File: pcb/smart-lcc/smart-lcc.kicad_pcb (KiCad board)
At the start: 2 copper layers, 53.2 x 53.2 mm, 4 parts

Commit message: Work on PCB
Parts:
- added C1: 2.2 µF / 25V, Capacitor_SMD:C_1206_3216Metric, F.Cu at (62.5, 36.6)
- added C2: 4.7µF / 25V, X7R, Capacitor_SMD:C_1206_3216Metric, F.Cu at (62.6, 32.8)
- added C3: 0.1 µF / 25V, X7R, Capacitor_SMD:C_0603_1608Metric, F.Cu at (62.5, 30.6)
- added J3: Conn_01x24 (mirrored), Connector_FFC-FPC:Hirose_FH12-24S-0.5SH_1x24-1MP_P0.50mm_Horizontal, F.Cu at (49.6, 36.1)
- added R1: 2K2, Resistor_SMD:R_0402_1005Metric, F.Cu at (29.8, 36.4)
- added R2: 3K3, Resistor_SMD:R_0402_1005Metric, F.Cu at (32.3, 36.4)
- added R3: 910K, Resistor_SMD:R_0603_1608Metric, F.Cu at (62.5, 39.2)
- added REF**: MountingHole_2.7mm, MountingHole:MountingHole_2.7mm, F.Cu at (33.5, 25.0)
- added REF**: MountingHole_2.7mm, MountingHole:MountingHole_2.7mm, F.Cu at (65.4, 25.0)
- added REF**: MountingHole_2.7mm, MountingHole:MountingHole_2.7mm, F.Cu at (70.2, 70.0)
- added REF**: MountingHole_2.7mm, MountingHole:MountingHole_2.7mm, F.Cu at (28.7, 70.0)
- added U1: ABX00027, ABX00027:MODULE_ABX00027, F.Cu at (53.9, 53.5)
- J1: renamed from REF**; value PinHeader_1x06_P2.54mm_Vertical -> Control board connector
- J2: renamed from REF**; value PinHeader_1x06_P2.54mm_Vertical -> Aux connector
- SW1, SW2: renamed from REF**; value SW_Push_1P1T_NO_6x6mm_H9.5mm -> SW_Push; moved to B.Cu
- moved J2 38.2 mm to (56.5, 73.4), turned to 270 degrees
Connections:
- J1 pad 1: (no net) -> +12V
- J1 pad 2: (no net) -> TX_TO_CONTROL_BOARD
- J1 pad 3: (no net) -> RX_FROM_CONTROL_BOARD_5V
- J1 pad 4: (no net) -> GND
- J1 pad 5: (no net) -> 3V3_OLED
- J1 pad 6: (no net) -> 3V3_MCU
- J2 pad 1: (no net) -> +12V
- J2 pad 2: (no net) -> RX_FROM_AUX
- J2 pad 3: (no net) -> TX_TO_AUX
- J2 pad 4: (no net) -> GND
- J2 pad 5: (no net) -> 3V3_OLED
- J2 pad 6: (no net) -> 3V3_MCU
- SW1 pad 1: (no net) -> +3V3
- SW1 pad 2: (no net) -> SW_MINUS
- SW2 pad 1: (no net) -> +3V3
- SW2 pad 2: (no net) -> SW_PLUS
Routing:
- net +12V: track 0.00 -> 122.0 mm
- net 3V3_OLED: track 0.00 -> 61.8 mm, vias 0 -> 1
- net GND: track 0.00 -> 46.9 mm, vias 0 -> 5
- net +3V3: track 0.00 -> 43.6 mm, vias 0 -> 1
- net SSD1309_CS: track 0.00 -> 36.9 mm
- net SSD1309_MOSI: track 0.00 -> 33.0 mm
- net 3V3_MCU: track 0.00 -> 32.5 mm
- net RX_FROM_CONTROL_BOARD_3V3: track 0.00 -> 30.5 mm
- net SSD1309_SCLK: track 0.00 -> 28.6 mm, vias 0 -> 2
- net TX_TO_CONTROL_BOARD: track 0.00 -> 25.4 mm
- net SW_MINUS: track 0.00 -> 22.7 mm, vias 0 -> 1
- net TX_TO_AUX: track 0.00 -> 21.9 mm
- net SW_PLUS: track 0.00 -> 17.5 mm, vias 0 -> 1
- net RX_FROM_AUX: track 0.00 -> 14.1 mm
- net RX_FROM_CONTROL_BOARD_5V: track 0.00 -> 12.4 mm, vias 0 -> 1
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- added copper zone on In1.Cu, net GND
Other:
- copper layers 2 -> 4
- net class 12V added: clearance 0.4, trace_width 0.5, via_dia 1.6, via_drill 0.8

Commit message: WIP
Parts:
- C3: footprint Capacitor_SMD:C_0603_1608Metric -> Capacitor_SMD:C_1206_3216Metric
- J1: footprint Connector_PinHeader_2.54mm:PinHeader_1x06_P2.54mm_Vertical -> TE_280372-1:TE_280372-1
- R1, R2: footprint Resistor_SMD:R_0402_1005Metric -> Resistor_SMD:R_0603_1608Metric
- moved J1 6.32 mm to (25.9, 45.3), turned to 270 degrees
- moved R2 4.06 mm to (36.3, 36.4)
- moved R1 2.92 mm to (32.8, 36.4)
- moved C3 0.76 mm to (62.5, 29.8)
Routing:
- net RX_FROM_CONTROL_BOARD_5V: track 12.4 -> 15.0 mm
- net RX_FROM_CONTROL_BOARD_3V3: track 30.5 -> 29.8 mm

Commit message: WIP
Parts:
- added JP1: SolderJumper_2_Open, Jumper:SolderJumper-2_P1.3mm_Open_RoundedPad1.0x1.5mm, F.Cu at (57.3, 68.6)
- added JP2: SolderJumper_2_Bridged, Jumper:SolderJumper-2_P1.3mm_Bridged_RoundedPad1.0x1.5mm, F.Cu at (41.2, 68.6)
- J1: value Control board connector -> 280372-1
- moved J1 47.1 mm to (73.0, 45.5)
- moved R1 45.1 mm to (72.1, 58.4), turned to 90 degrees
- moved R2 43.1 mm to (71.2, 61.7), turned to 0 degrees
- moved U1 8.33 mm to (45.6, 52.8), turned to 0 degrees
- moved C2 0.27 mm to (62.5, 33.0), turned to 180 degrees
- turned C3 to 180 degrees
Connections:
- U1 pad 10: SSD1309_DC -> Net-(U1-Pad10)
- U1 pad 11: SSD1309_RES -> Net-(U1-Pad11)
- U1 pad 15: +12V -> VIN
- U1 pad 20: Net-(U1-Pad20) -> SSD1309_DC
- U1 pad 21: Net-(U1-Pad21) -> SSD1309_RES
- U1 pad 22: SW_MINUS -> SW_PLUS
- U1 pad 23: SW_PLUS -> SW_MINUS
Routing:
- net +12V: track 122.3 -> 78.9 mm
- net RX_FROM_AUX: track 14.1 -> 36.5 mm
- net 3V3_OLED: track 61.8 -> 78.3 mm
- net SSD1309_CS: track 36.9 -> 20.6 mm
- net 3V3_MCU: track 32.5 -> 48.6 mm
- net TX_TO_AUX: track 21.9 -> 36.5 mm
- net TX_TO_CONTROL_BOARD: track 25.4 -> 10.9 mm
- net VIN: track 0.00 -> 10.0 mm
- net SSD1309_SCLK: track 28.6 -> 35.4 mm
- net GND: track 46.6 -> 53.4 mm, vias 5 -> 7
- net RX_FROM_CONTROL_BOARD_3V3: track 29.8 -> 23.1 mm
- net SSD1309_MOSI: track 33.0 -> 27.2 mm, vias 0 -> 2
- net SW_PLUS: track 17.5 -> 23.3 mm
- net +3V3: track 43.6 -> 48.6 mm
- net SW_MINUS: track 22.7 -> 21.4 mm
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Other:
- net class 12V: clearance 0.4 -> 0.2
- board text added: "Smart LCC"
- board text added: "github.com/magnusnordlander/smart-lcc"

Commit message: Getting ready to manufacture PCB
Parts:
- R1, R2, R3: footprint Resistor_SMD:R_0603_1608Metric -> Resistor_SMD:R_1206_3216Metric
- SW1, SW2: footprint Button_Switch_SMD:SW_Push_1P1T_NO_6x6mm_H9.5mm -> SW_Push_ADTSMW65:ADTSMW65
- moved C2 29.1 mm to (33.5, 35.8)
- moved C3 29.1 mm to (33.6, 32.7)
- moved C1 3.80 mm to (64.7, 33.5)
- moved R3 3.33 mm to (64.7, 36.8)
- moved R2 1.29 mm to (71.5, 63.0)
- moved R1 1.13 mm to (73.3, 58.2)
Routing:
- net +12V: track 78.9 -> 113.8 mm
- net Net-(C1-Pad1): track 9.07 -> 14.1 mm
- net Net-(J3-Pad4): track 9.56 -> 12.2 mm
- net RX_FROM_CONTROL_BOARD_3V3: track 23.1 -> 25.4 mm
- net RX_FROM_CONTROL_BOARD_5V: track 14.7 -> 13.5 mm
- net GND: track 53.4 -> 54.7 mm

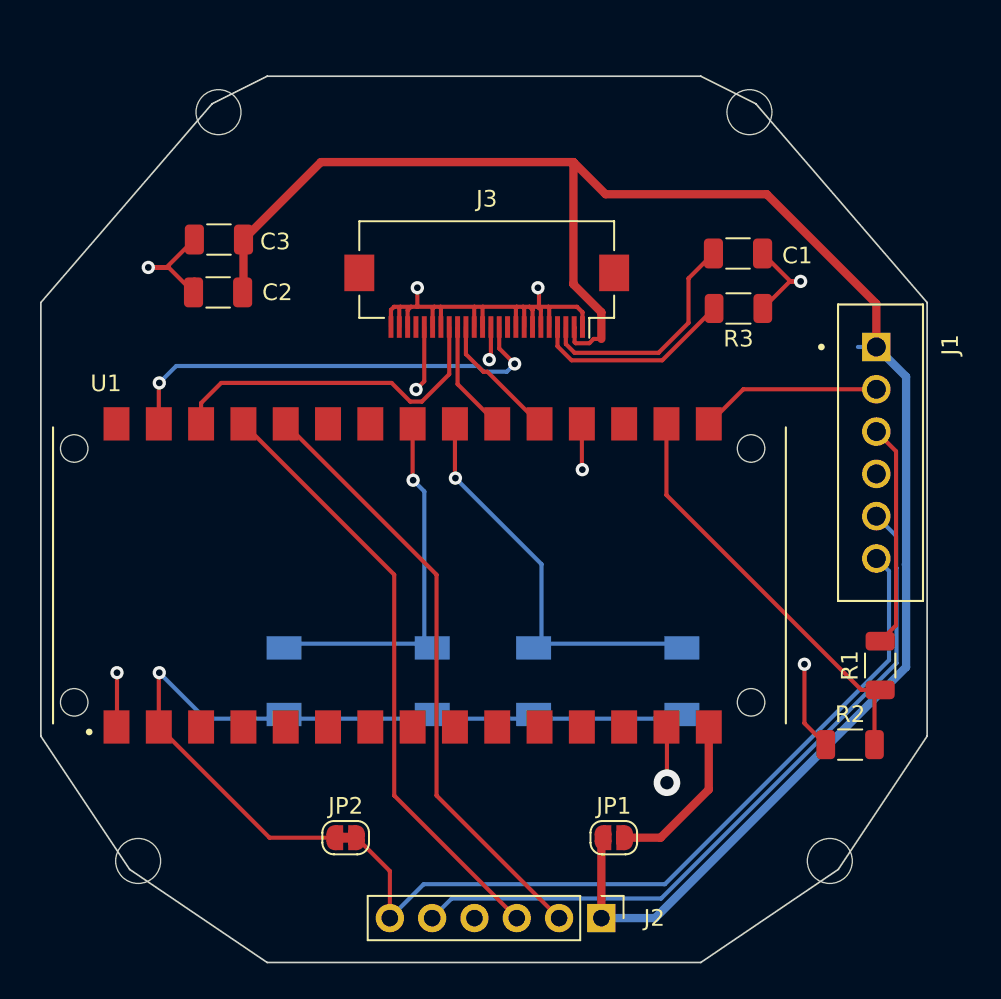
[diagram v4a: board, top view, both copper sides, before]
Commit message: Started work on a rev b board
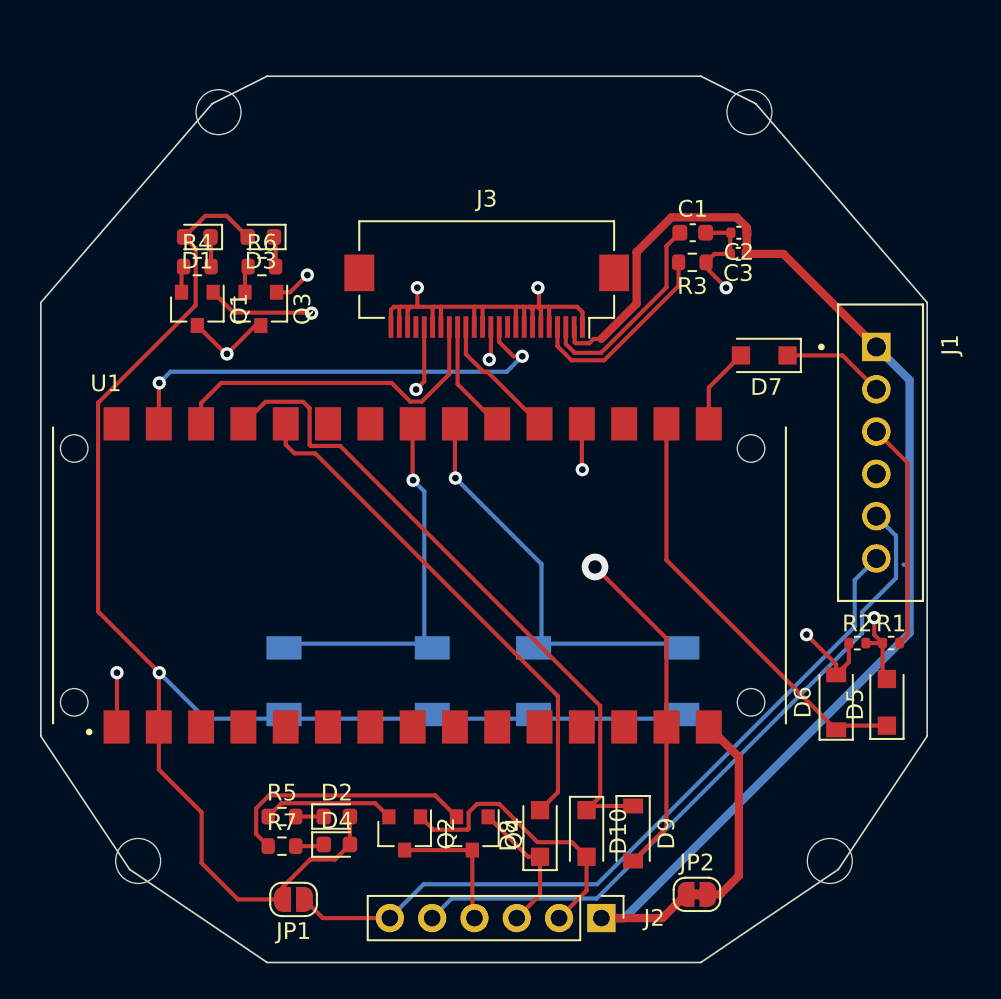
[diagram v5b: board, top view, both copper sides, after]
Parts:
- added D1: 19-217/BHC-ZL1M2RY/3T, LED_SMD:LED_0603_1608Metric, F.Cu at (32.3, 32.5)
- added D10: D_Small, Diode_SMD:D_SOD-123F, F.Cu at (55.6, 68.3)
- added D2: 19-217/BHC-ZL1M2RY/3T, LED_SMD:LED_0603_1608Metric, F.Cu at (40.6, 67.3)
- added D3: 19-217/BHC-ZL1M2RY/3T, LED_SMD:LED_0603_1608Metric, F.Cu at (36.1, 32.5)
- added D4: 19-217/BHC-ZL1M2RY/3T, LED_SMD:LED_0603_1608Metric, F.Cu at (40.6, 69.0)
- added D5: D_Small, Diode_SMD:D_SOD-123F, F.Cu at (73.7, 60.5)
- added D6: D_Zener_Small, Diode_SMD:D_SOD-123, F.Cu at (70.6, 60.5)
- added D7: D_Small, Diode_SMD:D_SOD-123F, F.Cu at (66.3, 39.6)
- added D8: D_Small, Diode_SMD:D_SOD-123F, F.Cu at (52.8, 68.3)
- added D9: D_Zener_Small, Diode_SMD:D_SOD-123, F.Cu at (58.4, 68.3)
- added Q1: MMBT3906, Package_TO_SOT_SMD:SOT-23, F.Cu at (32.3, 36.8)
- added Q2: MMBT3906, Package_TO_SOT_SMD:SOT-23, F.Cu at (44.7, 68.3)
- added Q3: MMBT3906, Package_TO_SOT_SMD:SOT-23, F.Cu at (36.1, 36.8)
- added Q4: MMBT3906, Package_TO_SOT_SMD:SOT-23, F.Cu at (48.8, 68.3)
- added R4: 20R, Resistor_SMD:R_0603_1608Metric, F.Cu at (32.3, 34.3)
- added R5: 20R, Resistor_SMD:R_0603_1608Metric, F.Cu at (37.3, 67.3)
- added R6: 20R, Resistor_SMD:R_0603_1608Metric, F.Cu at (36.1, 34.3)
- added R7: 20R, Resistor_SMD:R_0603_1608Metric, F.Cu at (37.3, 69.1)
- C1: footprint Capacitor_SMD:C_1206_3216Metric -> Capacitor_SMD:C_0603_1608Metric
- C2, C3: footprint Capacitor_SMD:C_1206_3216Metric -> Capacitor_SMD:C_0402_1005Metric
- R1, R2: footprint Resistor_SMD:R_1206_3216Metric -> Resistor_SMD:R_0402_1005Metric
- R3: footprint Resistor_SMD:R_1206_3216Metric -> Resistor_SMD:R_0603_1608Metric
- moved C2 31.5 mm to (64.8, 32.3)
- moved C3 31.2 mm to (64.7, 33.5)
- moved JP2 21.4 mm to (62.3, 72.0)
- moved JP1 19.6 mm to (38.0, 72.3), turned to 180 degrees
- moved R2 6.11 mm to (71.9, 56.9)
- moved R3 3.92 mm to (62.0, 34.0)
- moved C1 2.99 mm to (62.0, 32.3)
- moved R1 1.50 mm to (73.9, 56.9), turned to 0 degrees
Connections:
- JP1 pad 1: +12V -> 3V3_MCU
- JP1 pad 2: VIN -> +3V3
- JP2 pad 1: 3V3_MCU -> VIN
- JP2 pad 2: +3V3 -> +12V
- U1 pad 16: TX_TO_CONTROL_BOARD -> Net-(D7-Pad2)
- U1 pad 17: RX_FROM_CONTROL_BOARD_3V3 -> Net-(D5-Pad1)
- U1 pad 26: RX_FROM_AUX -> Net-(D8-Pad2)
- U1 pad 27: TX_TO_AUX -> Net-(D10-Pad1)
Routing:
- net +3V3: track 48.6 -> 93.1 mm
- net Net-(D10-Pad1): track 0.00 -> 40.3 mm
- net +12V: track 113.8 -> 77.7 mm
- net TX_TO_CONTROL_BOARD: track 10.9 -> 45.4 mm, vias 0 -> 1
- net RX_FROM_CONTROL_BOARD_3V3: track 25.4 -> 58.5 mm, vias 0 -> 2
- net Net-(D8-Pad2): track 0.00 -> 31.1 mm
- net TX_TO_AUX: track 36.5 -> 8.37 mm
- net Net-(D5-Pad1): track 0.00 -> 25.7 mm
- net GND: track 54.7 -> 78.1 mm
- net RX_FROM_AUX: track 36.5 -> 17.2 mm
- net Net-(Q4-Pad2): track 0.00 -> 15.5 mm
- net Net-(Q2-Pad2): track 0.00 -> 7.91 mm
- net Net-(D7-Pad2): track 0.00 -> 4.91 mm
- net 3V3_MCU: track 48.6 -> 45.5 mm
- net 3V3_OLED: track 78.3 -> 76.0 mm
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
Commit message: WIP
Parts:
- removed D10: D_Small, Diode_SMD:D_SOD-123F
- removed D9: D_Zener_Small, Diode_SMD:D_SOD-123
- added R3: 220R, Resistor_SMD:R_0402_1005Metric, F.Cu at (67.8, 38.4)
- added R4: 220R, Resistor_SMD:R_0402_1005Metric, F.Cu at (52.0, 67.5)
- added R5: 220R, Resistor_SMD:R_0402_1005Metric, F.Cu at (58.6, 67.5)
- added REF**: OSHW-Logo2_7.3x6mm_SilkScreen, Symbol:OSHW-Logo2_7.3x6mm_SilkScreen, F.Cu at (32.8, 52.6)
- C1: footprint Capacitor_SMD:C_0603_1608Metric -> Capacitor_SMD:C_0805_2012Metric
- C2: footprint Capacitor_SMD:C_0402_1005Metric -> Capacitor_SMD:C_1206_3216Metric
- C3: footprint Capacitor_SMD:C_0402_1005Metric -> Capacitor_SMD:C_0603_1608Metric
- D5, D7, D8: value D_Small -> D_Zener_Small; footprint Diode_SMD:D_SOD-123F -> Diode_SMD:D_SOD-123
- H1, H2, H3, H4: renamed from REF**; value MountingHole_2.7mm -> MountingHole
- J3: value Conn_01x24 (mirrored) -> Conn_01x24; footprint Connector_FFC-FPC:Hirose_FH12-24S-0.5SH_1x24-1MP_P0.50mm_Horizontal -> FH34SRJ-24S-0.5SH_50:FH34SRJ24S05SH50
- Q1, Q2, Q3, Q4: value MMBT3906 -> 2N7002
- moved Q2 32.7 mm to (36.1, 36.8), turned to 90 degrees
- moved Q3 32.7 mm to (44.7, 68.3), turned to 90 degrees
- moved D7 30.5 mm to (53.9, 67.6), turned to 270 degrees
- moved D6 24.5 mm to (65.3, 36.6)
- moved C2 4.79 mm to (60.7, 29.7), turned to 90 degrees
- moved D8 3.89 mm to (56.6, 67.6), turned to 270 degrees
- moved R10 3.89 mm to (61.2, 37.8)
- moved C3 3.64 mm to (62.7, 30.5), turned to 90 degrees
- moved C1 3.64 mm to (61.2, 35.8)
- moved R8 2.23 mm to (36.3, 67.1), turned to 180 degrees
- moved D3 2.09 mm to (39.6, 67.2), turned to 180 degrees
- moved R7 2.03 mm to (36.1, 32.3)
- moved R6 2.03 mm to (32.3, 32.3)
- moved R9 1.87 mm to (36.3, 68.9), turned to 180 degrees
- moved D4 1.82 mm to (39.6, 68.8), turned to 180 degrees
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- renumbered D3 to D2, D4 to D3, D2 to D4, R3 to R10, R4 to R6, R6 to R7, R7 to R8, R5 to R9, SW2 to SW1, SW1 to SW2
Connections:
- D1 pad 2: +3V3 -> Net-(D1-Pad2)
- D2 pad 1: Net-(D3-Pad1) -> Net-(D2-Pad1)
- D2 pad 2: +3V3 -> Net-(D2-Pad2)
- D3 pad 1: Net-(D4-Pad1) -> Net-(D3-Pad1)
- D3 pad 2: +3V3 -> Net-(D3-Pad2)
- D4 pad 1: Net-(D2-Pad1) -> Net-(D4-Pad1)
- D4 pad 2: +3V3 -> Net-(D4-Pad2)
- D5 pad 1: Net-(D5-Pad1) -> RX_FROM_CONTROL_BOARD_3V3
- D5 pad 2: RX_FROM_CONTROL_BOARD_3V3 -> GND
- D6 pad 1: Net-(D5-Pad1) -> Net-(D6-Pad1)
- D7 pad 1: TX_TO_CONTROL_BOARD -> Net-(D7-Pad1)
- D7 pad 2: Net-(D7-Pad2) -> GND
- D8 pad 1: TX_TO_AUX -> Net-(D8-Pad1)
- D8 pad 2: Net-(D8-Pad2) -> GND
- J3 pad 10: Net-(J3-Pad10) -> SSD1309_DC
- J3 pad 11: SSD1309_MOSI -> GND
- J3 pad 12: SSD1309_SCLK -> GND
- J3 pad 13: GND -> SSD1309_SCLK
- J3 pad 14: GND -> SSD1309_MOSI
- J3 pad 15: SSD1309_DC -> (no net)
- J3 pad 16: SSD1309_RES -> GND
- J3 pad 17: SSD1309_CS -> GND
- J3 pad 2: +12V -> GND
- J3 pad 20: 3V3_OLED -> GND
- J3 pad 22: GND -> Net-(C1-Pad1)
- J3 pad 23: GND -> +12V
- J3 pad 3: Net-(C1-Pad1) -> GND
- J3 pad 4: Net-(J3-Pad4) -> (no net)
- J3 pad 5: GND -> 3V3_OLED
- J3 pad 8: GND -> SSD1309_CS
- J3 pad 9: GND -> SSD1309_RES
- Q1 pad 2: Net-(Q1-Pad2) -> GND
- Q1 pad 3: GND -> Net-(D1-Pad1)
- Q2 pad 1: RX_FROM_AUX -> TX_TO_CONTROL_BOARD
- Q2 pad 2: Net-(Q2-Pad2) -> GND
- Q2 pad 3: GND -> Net-(D2-Pad1)
- Q3 pad 1: TX_TO_CONTROL_BOARD -> RX_FROM_AUX
- Q3 pad 2: Net-(Q3-Pad2) -> GND
- Q3 pad 3: GND -> Net-(D3-Pad1)
- Q4 pad 2: Net-(Q4-Pad2) -> GND
- Q4 pad 3: GND -> Net-(D4-Pad1)
- R10 pad 2: Net-(J3-Pad4) -> Net-(J3-Pad21)
- R6 pad 1: Net-(Q1-Pad2) -> Net-(D1-Pad2)
- R6 pad 2: Net-(D1-Pad1) -> +3V3
- R7 pad 1: Net-(Q3-Pad2) -> Net-(D2-Pad2)
- R7 pad 2: Net-(D3-Pad1) -> +3V3
- R8 pad 1: Net-(Q4-Pad2) -> Net-(D3-Pad2)
- R8 pad 2: Net-(D4-Pad1) -> +3V3
- R9 pad 1: Net-(Q2-Pad2) -> Net-(D4-Pad2)
- R9 pad 2: Net-(D2-Pad1) -> +3V3
- U1 pad 10: Net-(U1-Pad10) -> (no net)
- U1 pad 11: Net-(U1-Pad11) -> (no net)
- U1 pad 12: Net-(U1-Pad12) -> (no net)
- U1 pad 16: Net-(D7-Pad2) -> Net-(D6-Pad1)
- U1 pad 17: Net-(D5-Pad1) -> RX_FROM_CONTROL_BOARD_3V3
- U1 pad 24: Net-(U1-Pad24) -> (no net)
- U1 pad 25: Net-(U1-Pad25) -> (no net)
- U1 pad 26: Net-(D8-Pad2) -> Net-(D7-Pad1)
- U1 pad 27: Net-(D10-Pad1) -> Net-(D8-Pad1)
- U1 pad 3: Net-(U1-Pad3) -> (no net)
- U1 pad 30: Net-(U1-Pad30) -> (no net)
- U1 pad 4: Net-(U1-Pad4) -> (no net)
- U1 pad 5: Net-(U1-Pad5) -> (no net)
- U1 pad 6: Net-(U1-Pad6) -> (no net)
- U1 pad 7: Net-(U1-Pad7) -> (no net)
- U1 pad 8: Net-(U1-Pad8) -> (no net)
- U1 pad 9: Net-(U1-Pad9) -> (no net)
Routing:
- net Net-(D10-Pad1): track 40.3 -> 0.00 mm
- net Net-(D8-Pad1): track 0.00 -> 38.7 mm
- net Net-(D7-Pad1): track 0.00 -> 32.2 mm
- net Net-(D8-Pad2): track 31.1 -> 0.00 mm
- net RX_FROM_CONTROL_BOARD_3V3: track 58.5 -> 84.7 mm
- net Net-(D5-Pad1): track 25.7 -> 0.00 mm
- net Net-(Q4-Pad2): track 15.5 -> 0.00 mm
- net Net-(J3-Pad4): track 12.0 -> 0.00 mm
- net Net-(D4-Pad1): track 1.72 -> 12.1 mm
- net Net-(D6-Pad1): track 0.00 -> 9.20 mm
- net Net-(J3-Pad21): track 0.00 -> 8.87 mm
- net Net-(Q2-Pad2): track 7.91 -> 0.00 mm
- net Net-(D7-Pad2): track 4.91 -> 0.00 mm
- net RX_FROM_AUX: track 17.2 -> 21.7 mm
- net Net-(C1-Pad1): track 12.5 -> 8.64 mm
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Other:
- board text added: "12V"
- board text added: "3V3 MCU"
- board text added: "3V3 OLED"
- board text added: "Aux"
- board text added: "GND"
- board text added: "Licensed under CERN-OHL-P v2"
- board text added: "Minus"
- board text added: "Plus"
- board text added: "RX"
- board text added: "Rev B"
- board text added: "TX"

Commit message: Rev B as sent to manufacturing
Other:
- board text added: "K"
